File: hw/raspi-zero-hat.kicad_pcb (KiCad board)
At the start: 2 copper layers, 65 x 63 mm, 44 parts, among them J1 Screw_Terminal_01x02, J2 Screw_Terminal_01x03, K1 G5LE-1, P1 Conn_02x20_Odd_Even, Q1 MMBT3904

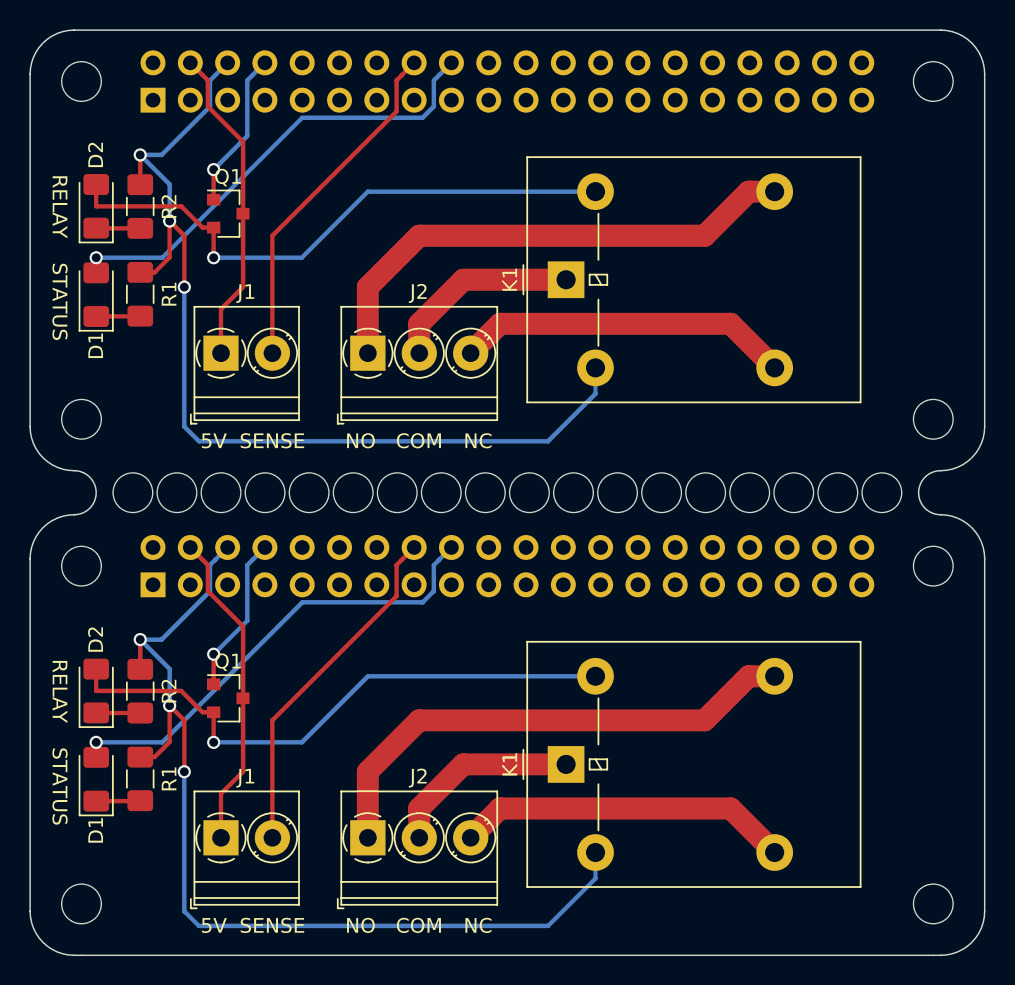
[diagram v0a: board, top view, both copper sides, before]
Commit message: moved relay control pin to pin 10 (pin 8 was pulled up on boot, causing an unintended relay toggle).
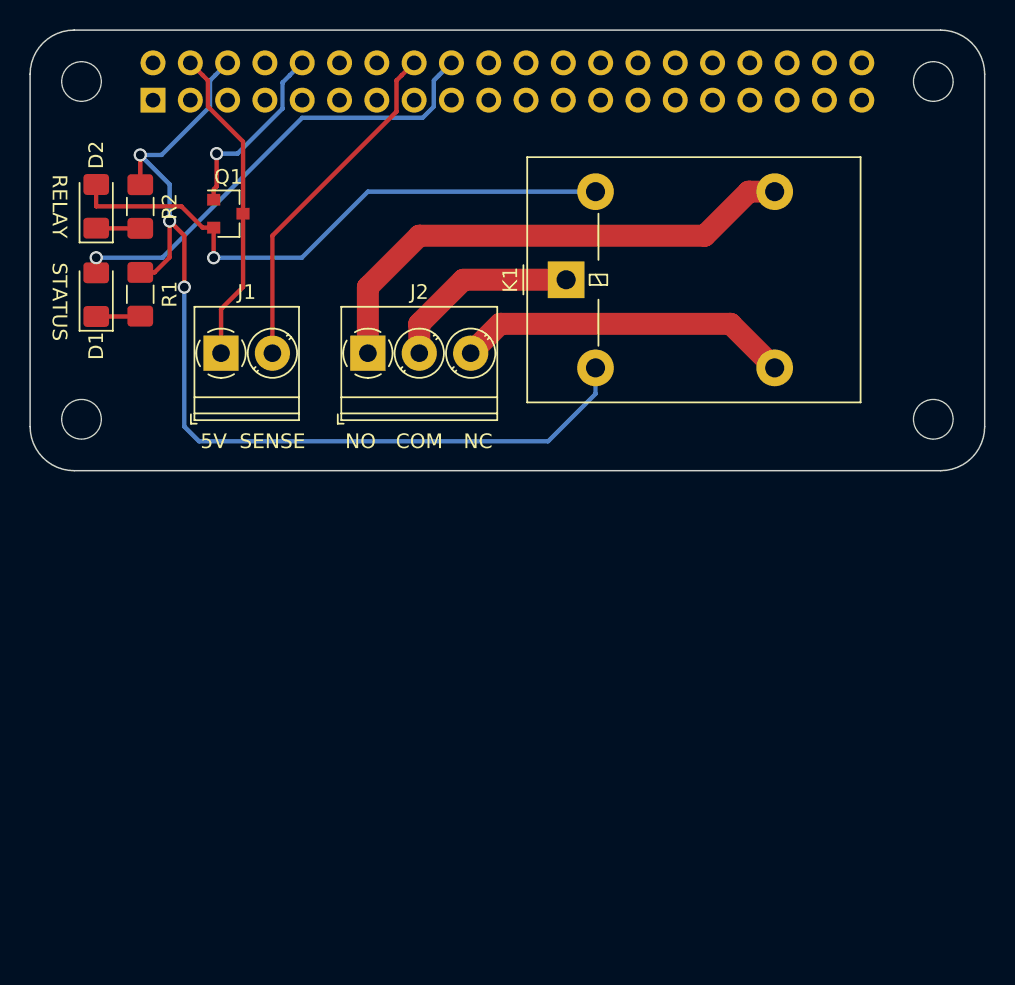
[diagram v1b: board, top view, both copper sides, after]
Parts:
- removed the D1 at (204.5, 171.0)
- removed the D2 at (204.5, 165.0)
- removed the J1 at (213.0, 175.0)
- removed the J2 at (223.0, 175.0)
- removed the K1 at (236.5, 170.0)
- removed the MK1 at (203.5, 156.5)
- removed the MK1 at (234.0, 151.5)
- removed the MK1 at (228.0, 151.5)
- removed the MK1 at (225.0, 151.5)
- removed the MK1 at (231.0, 151.5)
- removed the MK1 at (222.0, 151.5)
- removed the MK1 at (219.0, 151.5)
- removed the MK1 at (216.0, 151.5)
- removed the MK1 at (213.0, 151.5)
- removed the MK1 at (210.0, 151.5)
- removed the MK1 at (207.0, 151.5)
- removed the MK1 at (258.0, 151.5)
- removed the MK1 at (252.0, 151.5)
- removed the MK1 at (255.0, 151.5)
- removed the MK1 at (237.0, 151.5)
- removed the MK1 at (243.0, 151.5)
- removed the MK1 at (249.0, 151.5)
- removed the MK1 at (246.0, 151.5)
- removed the MK1 at (240.0, 151.5)
- removed the MK2 at (261.5, 156.5)
- removed the MK3 at (203.5, 179.5)
- removed the MK4 at (261.5, 179.5)
- removed the P1 at (208.4, 157.8)
- removed the Q1 at (213.5, 165.5)
- removed the R1 at (207.5, 171.0)
- removed the R2 at (207.5, 165.0)
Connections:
- P1 pad 8: /GPIO14(TXD0) -> Net-(P1-Pad8)
- Q1 pad 1: /GPIO14(TXD0) -> /GPIO15(RXD0)
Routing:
- net GND: track 135.6 -> 67.8 mm, vias 6 -> 3
- net Net-(D2-Pad2): track 80.0 -> 40.0 mm, vias 2 -> 1
- net Net-(J2-Pad1): track 69.8 -> 34.9 mm
- net /GPIO24(GEN5): track 63.5 -> 31.8 mm, vias 2 -> 1
- net /GPIO23(GEN4): track 47.5 -> 23.8 mm
- net Net-(J2-Pad3): track 45.5 -> 22.8 mm
- net +5V: track 43.8 -> 21.9 mm
- net /GPIO14(TXD0): track 21.5 -> 0.00 mm, vias 2 -> 0
- net Net-(J2-Pad2): track 26.5 -> 13.2 mm
- net /GPIO15(RXD0): track 0.00 -> 12.7 mm, vias 0 -> 1
- net Net-(D1-Pad1): track 6.02 -> 3.01 mm
- net Net-(D2-Pad1): track 6.01 -> 3.01 mm
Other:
- board size 65 x 63 mm -> 65 x 30 mm
